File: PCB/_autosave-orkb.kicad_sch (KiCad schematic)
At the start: 82 parts, among them J1 USB_C_Receptacle_USB2.0, P1 OLED, SW1 MXHS, SW10 MXHS, SW11 MXHS, SW12 MXHS, SW13 MXHS, SW14 MXHS, SW15 MXHS, SW16 MXHS, SW17 MXHS, SW18 MXHS, SW19 MXHS, SW2 MXHS, SW20 MXHS, SW21 MXHS, SW22 MXHS, SW23 MXHS, SW3 MXHS, SW4 MXHS, SW5 MXHS, SW6 MXHS, SW7 MXHS, SW8 MXHS, SW9 MXHS, U1 ProMicro, U2 SRV05-4, U3 SRV05-4

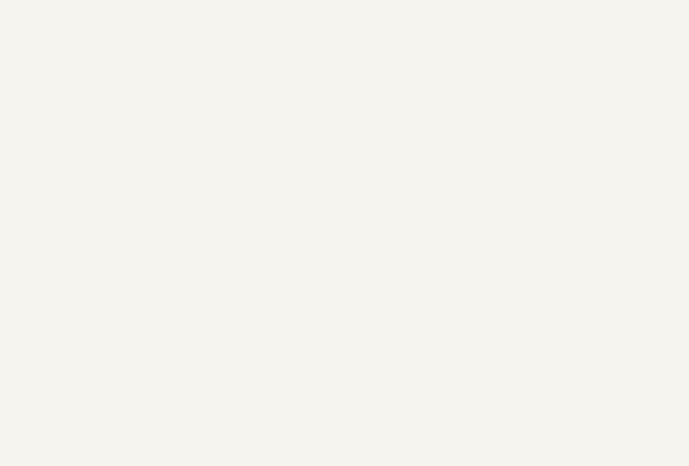
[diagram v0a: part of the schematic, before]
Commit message: Changing layout and adding space for a three way switch
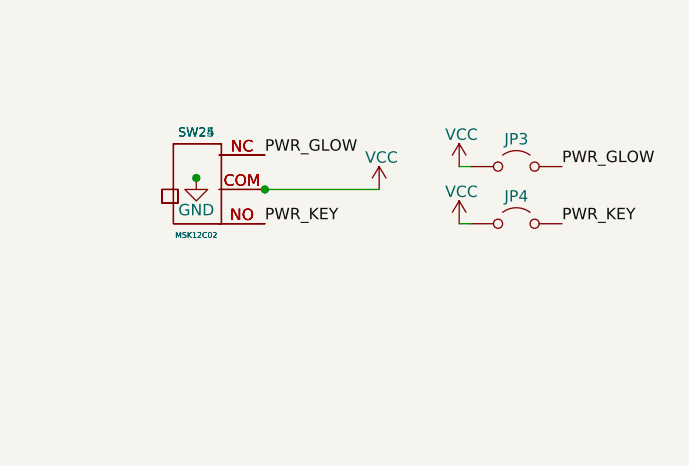
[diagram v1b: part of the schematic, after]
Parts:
- added JP3, JP4: Jumper_2_Open, SplitKeyboard_Common:Jumper_min_v2, symbol Jumper:Jumper_2_Open
- added SW24, SW25: MSK12C02, SplitKeyboard_Common:MSK12C02, symbol SplitKeyboard_Common:MSK12C02
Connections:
- net GND: now also SW24.MP (GND), SW25.MP (GND)
- net VCC: now also JP3.1 (A), JP4.1 (A), SW24.COM, SW25.COM
- new net PWR_GLOW: JP3.2 (B), SW24.NC, SW25.NC
- new net PWR_KEY: JP4.2 (B), SW24.NO, SW25.NO
